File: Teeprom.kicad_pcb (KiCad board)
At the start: 2 copper layers, 16 x 38 mm, 4 parts, among them J1 Tandy_100_102_200_option_rom, U1 28C256

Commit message: improve pour
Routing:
- net /A10: track 22.2 -> 20.9 mm
- net /A6: track 6.71 -> 6.08 mm
- net /VSS: vias 6 -> 5
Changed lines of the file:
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@@
     (thickness 1.6)
     (drawings 11)
-    (tracks 140)
+    (tracks 137)
     (zones 0)
     (modules 4)
@@
   (via (at 151.9184 99.822) (size 0.508) (drill 0.254) (layers Top Bottom) (net 2))
   (segment (start 138.811 85.217) (end 138.7094 85.217) (width 0.2032) (layer Bottom) (net 2))
-  (segment (start 150.368 99.822) (end 144.0942 93.5482) (width 0.2032) (layer Bottom) (net 2))
-  (segment (start 144.0942 93.5482) (end 142.0876 93.5482) (width 0.2032) (layer Bottom) (net 2))
-  (segment (start 151.9184 99.822) (end 150.368 99.822) (width 0.2032) (layer Bottom) (net 2))
+  (segment (start 151.9184 99.822) (end 150.6474 99.822) (width 0.2032) (layer Bottom) (net 2))
   (segment (start 141.4526 87.8586) (end 138.811 85.217) (width 0.2032) (layer Bottom) (net 2))
-  (segment (start 142.0876 93.5482) (end 141.4526 92.9132) (width 0.2032) (layer Bottom) (net 2))
-  (segment (start 141.4526 92.9132) (end 141.4526 87.8586) (width 0.2032) (layer Bottom) (net 2))
+  (segment (start 141.4526 90.6272) (end 141.4526 87.8586) (width 0.2032) (layer Bottom) (net 2))
+  (segment (start 150.6474 99.822) (end 141.4526 90.6272) (width 0.2032) (layer Bottom) (net 2))
   (via (at 151.9174 106.172) (size 0.508) (drill 0.254) (layers Top Bottom) (net 3))
   (segment (start 151.9174 109.4613) (end 151.9174 106.172) (width 0.2032) (layer Bottom) (net 3))
@@
   (segment (start 155.575 110.617) (end 153.7462 108.7882) (width 0.2032) (layer Top) (net 5))
   (via (at 142.5194 94.742) (size 0.508) (drill 0.254) (layers Top Bottom) (net 6))
-  (segment (start 140.4747 93.7768) (end 141.4399 94.742) (width 0.2032) (layer Bottom) (net 6))
-  (segment (start 140.4747 91.96705) (end 140.4747 93.7768) (width 0.2032) (layer Bottom) (net 6))
+  (segment (start 140.716 92.9386) (end 142.5194 94.742) (width 0.2032) (layer Bottom) (net 6))
+  (segment (start 140.716 92.20835) (end 140.716 92.9386) (width 0.2032) (layer Bottom) (net 6))
   (segment (start 138.7094 90.297) (end 138.80465 90.297) (width 0.2032) (layer Bottom) (net 6))
-  (segment (start 141.4399 94.742) (end 142.5194 94.742) (width 0.2032) (layer Bottom) (net 6))
-  (segment (start 138.80465 90.297) (end 140.4747 91.96705) (width 0.2032) (layer Bottom) (net 6))
+  (segment (start 138.80465 90.297) (end 140.716 92.20835) (width 0.2032) (layer Bottom) (net 6))
   (via (at 151.9174 103.632) (size 0.508) (drill 0.254) (layers Top Bottom) (net 7))
   (segment (start 153.6065 105.3211) (end 151.9174 103.632) (width 0.2032) (layer Bottom) (net 7))
@@
   (segment (start 138.7094 105.537) (end 138.8745 105.537) (width 0.2032) (layer Top) (net 17))
   (segment (start 138.8745 105.537) (end 140.6906 103.7209) (width 0.2032) (layer Top) (net 17))
-  (via (at 142.5184 92.202) (size 0.508) (drill 0.254) (layers Top Bottom) (net 18))
   (segment (start 155.0924 92.202) (end 155.7274 92.837) (width 0.2032) (layer Bottom) (net 18))
-  (segment (start 142.5184 92.202) (end 155.0924 92.202) (width 0.2032) (layer Bottom) (net 18))
+  (via (at 145.9484 92.202) (size 0.508) (drill 0.254) (layers Top Bottom) (net 18))
+  (segment (start 145.9484 92.202) (end 155.0924 92.202) (width 0.2032) (layer Bottom) (net 18))
+  (segment (start 142.5184 92.202) (end 145.9484 92.202) (width 0.2032) (layer Top) (net 18))
   (via (at 142.5194 103.632) (size 0.508) (drill 0.254) (layers Top Bottom) (net 19))
   (segment (start 141.0208 105.1306) (end 142.5194 103.632) (width 0.2032) (layer Bottom) (net 19))
@@
   (segment (start 155.1199 85.9155) (end 149.1107 85.9155) (width 0.2032) (layer Top) (net 24))
   (segment (start 148.0058 87.0204) (end 148.0058 98.3742) (width 0.2032) (layer Top) (net 24))
-  (segment (start 155.0289 83.3755) (end 149.5679 83.3755) (width 0.2032) (layer Top) (net 25))
+  (segment (start 143.5481 90.932) (end 142.5184 90.932) (width 0.2032) (layer Top) (net 25))
+  (segment (start 149.8346 83.3755) (end 143.9164 89.2937) (width 0.2032) (layer Top) (net 25))
+  (segment (start 155.0289 83.3755) (end 149.8346 83.3755) (width 0.2032) (layer Top) (net 25))
+  (segment (start 143.9164 89.2937) (end 143.9164 90.5637) (width 0.2032) (layer Top) (net 25))
   (segment (start 155.7274 82.677) (end 155.0289 83.3755) (width 0.2032) (layer Top) (net 25))
-  (segment (start 149.5679 83.3755) (end 146.5072 86.4362) (width 0.2032) (layer Top) (net 25))
-  (segment (start 143.5481 90.932) (end 142.5184 90.932) (width 0.2032) (layer Top) (net 25))
-  (segment (start 146.5072 87.9729) (end 143.5481 90.932) (width 0.2032) (layer Top) (net 25))
-  (segment (start 146.5072 86.4362) (end 146.5072 87.9729) (width 0.2032) (layer Top) (net 25))
+  (segment (start 143.9164 90.5637) (end 143.5481 90.932) (width 0.2032) (layer Top) (net 25))
   (segment (start 150.5991 89.1007) (end 150.5991 88.7984) (width 0.2032) (layer Top) (net 26))
   (segment (start 150.3553 89.3445) (end 150.5991 89.1007) (width 0.2032) (layer Top) (net 26))
@@
   (segment (start 151.9184 92.202) (end 150.9268 92.202) (width 0.2032) (layer Top) (net 26))
   (segment (start 150.9268 92.202) (end 150.3553 91.6305) (width 0.2032) (layer Top) (net 26))
-  (via (at 151.5491 89.9795) (size 0.508) (drill 0.254) (layers Top Bottom) (net 27))
   (via (at 149.7584 96.647) (size 0.508) (drill 0.254) (layers Top Bottom) (net 27))
-  (via (at 147.2184 106.807) (size 0.508) (drill 0.254) (layers Top Bottom) (net 27))
   (via (at 147.2184 82.677) (size 0.508) (drill 0.254) (layers Top Bottom) (net 27))
   (segment (start 142.5184 112.1547) (end 142.5184 107.442) (width 0.4064) (layer Top) (net 27))
   (segment (start 138.7094 115.697) (end 138.9761 115.697) (width 0.4064) (layer Top) (net 27))
   (segment (start 138.9761 115.697) (end 142.5184 112.1547) (width 0.4064) (layer Top) (net 27))
-  (via (at 147.2184 93.472) (size 0.508) (drill 0.254) (layers Top Bottom) (net 27))
-  (via (at 147.2184 89.027) (size 0.508) (drill 0.254) (layers Top Bottom) (net 27))
+  (via (at 147.2184 94.107) (size 0.508) (drill 0.254) (layers Top Bottom) (net 27))
+  (via (at 147.2184 87.757) (size 0.508) (drill 0.254) (layers Top Bottom) (net 27))
+  (via (at 151.5491 89.9414) (size 0.508) (drill 0.254) (layers Top Bottom) (net 27))
   (via (at 151.9184 90.932) (size 0.508) (drill 0.254) (layers Top Bottom) (net 28))
   (segment (start 138.9761 82.677) (end 138.6184 82.677) (width 0.4064) (layer Bottom) (net 28))

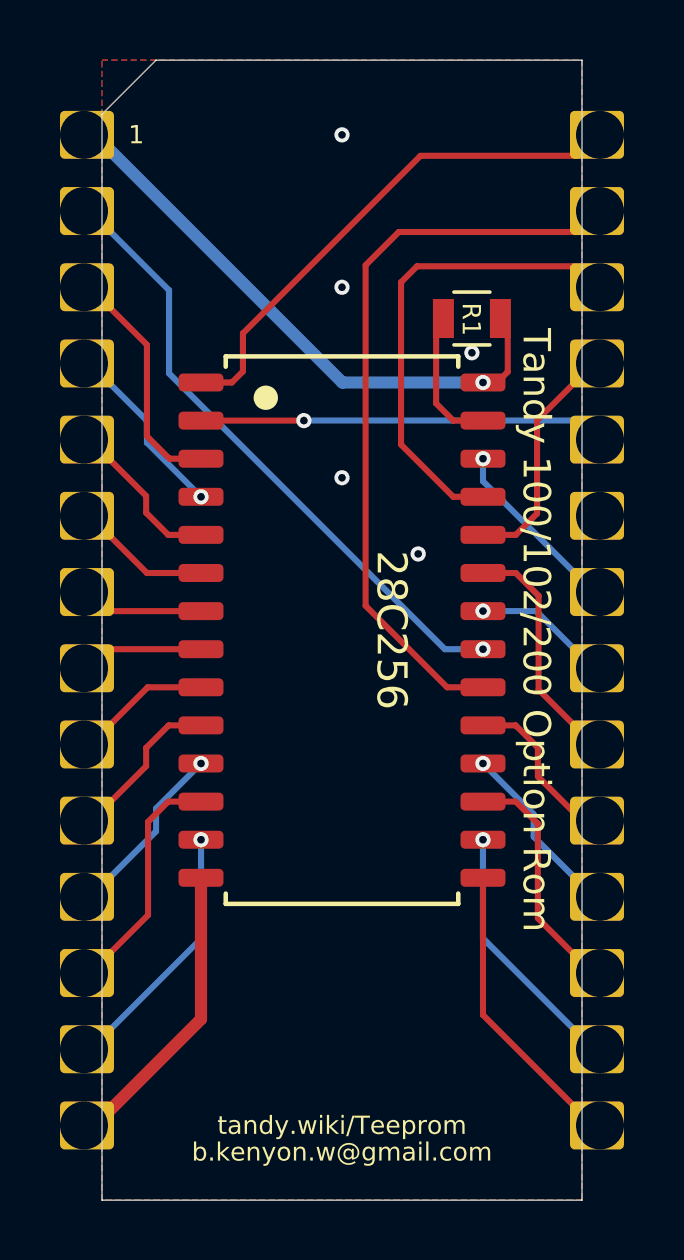
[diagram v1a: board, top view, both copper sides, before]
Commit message: improve ground paths in pours
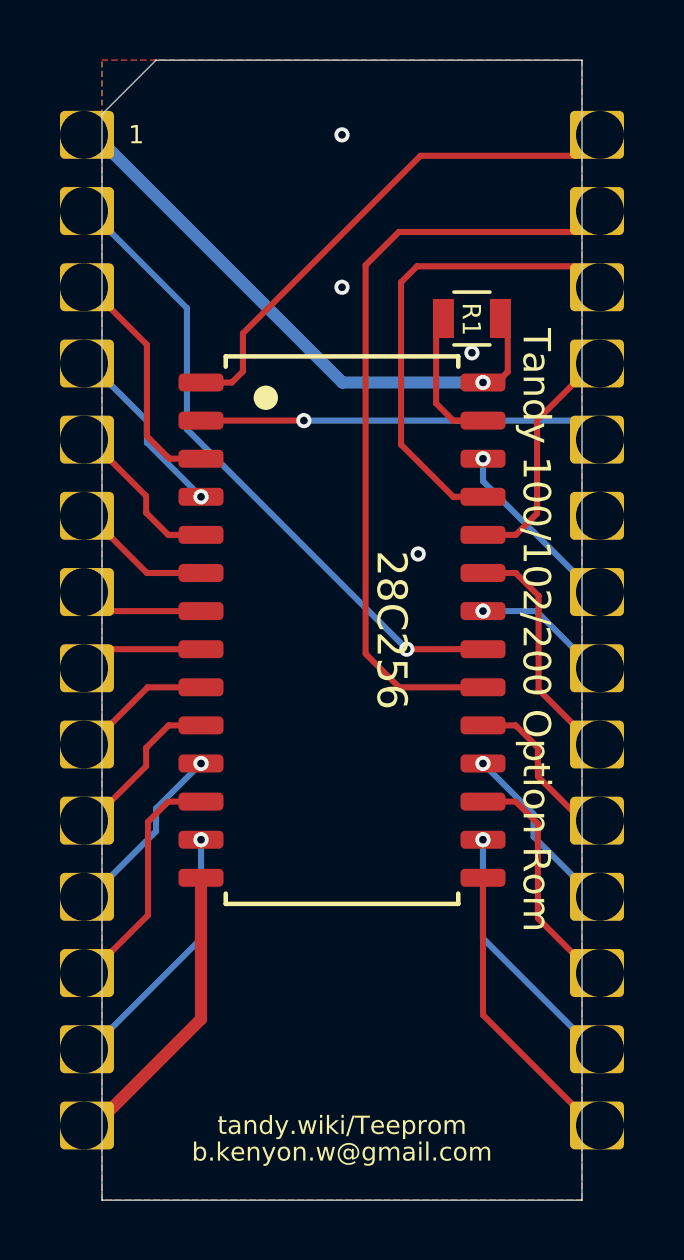
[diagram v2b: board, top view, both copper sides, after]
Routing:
- net /~CE: track 24.9 -> 25.9 mm
- net /A10: track 20.9 -> 21.6 mm
- net /VSS: vias 5 -> 4
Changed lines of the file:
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@@
     (thickness 1.6)
     (drawings 11)
-    (tracks 137)
+    (tracks 136)
     (zones 0)
     (modules 4)
@@
   (segment (start 155.7274 115.697) (end 155.6004 115.697) (width 0.2032) (layer Top) (net 1))
   (segment (start 155.6004 115.697) (end 151.9184 112.015) (width 0.2032) (layer Top) (net 1))
-  (via (at 151.9184 99.822) (size 0.508) (drill 0.254) (layers Top Bottom) (net 2))
+  (via (at 149.3774 99.822) (size 0.508) (drill 0.254) (layers Top Bottom) (net 2))
+  (segment (start 151.9184 99.822) (end 149.3774 99.822) (width 0.2032) (layer Top) (net 2))
   (segment (start 138.811 85.217) (end 138.7094 85.217) (width 0.2032) (layer Bottom) (net 2))
-  (segment (start 151.9184 99.822) (end 150.6474 99.822) (width 0.2032) (layer Bottom) (net 2))
-  (segment (start 141.4526 87.8586) (end 138.811 85.217) (width 0.2032) (layer Bottom) (net 2))
-  (segment (start 141.4526 90.6272) (end 141.4526 87.8586) (width 0.2032) (layer Bottom) (net 2))
-  (segment (start 150.6474 99.822) (end 141.4526 90.6272) (width 0.2032) (layer Bottom) (net 2))
+  (segment (start 149.3774 99.822) (end 142.0495 92.4941) (width 0.2032) (layer Bottom) (net 2))
+  (segment (start 142.0495 88.4555) (end 138.811 85.217) (width 0.2032) (layer Bottom) (net 2))
+  (segment (start 142.0495 92.4941) (end 142.0495 88.4555) (width 0.2032) (layer Bottom) (net 2))
   (via (at 151.9174 106.172) (size 0.508) (drill 0.254) (layers Top Bottom) (net 3))
   (segment (start 151.9174 109.4613) (end 151.9174 106.172) (width 0.2032) (layer Bottom) (net 3))
@@
   (segment (start 138.7094 113.157) (end 138.8364 113.157) (width 0.2032) (layer Bottom) (net 23))
   (segment (start 138.8364 113.157) (end 142.5194 109.474) (width 0.2032) (layer Bottom) (net 23))
-  (segment (start 150.7236 101.092) (end 151.9184 101.092) (width 0.2032) (layer Top) (net 24))
-  (segment (start 148.0058 98.3742) (end 150.7236 101.092) (width 0.2032) (layer Top) (net 24))
+  (segment (start 149.1234 101.092) (end 151.9184 101.092) (width 0.2032) (layer Top) (net 24))
   (segment (start 155.7274 85.308) (end 155.1199 85.9155) (width 0.2032) (layer Top) (net 24))
+  (segment (start 148.0058 99.9744) (end 149.1234 101.092) (width 0.2032) (layer Top) (net 24))
+  (segment (start 148.0058 87.0204) (end 148.0058 99.9744) (width 0.2032) (layer Top) (net 24))
   (segment (start 155.7274 85.217) (end 155.7274 85.308) (width 0.2032) (layer Top) (net 24))
   (segment (start 149.1107 85.9155) (end 148.0058 87.0204) (width 0.2032) (layer Top) (net 24))
   (segment (start 155.1199 85.9155) (end 149.1107 85.9155) (width 0.2032) (layer Top) (net 24))
-  (segment (start 148.0058 87.0204) (end 148.0058 98.3742) (width 0.2032) (layer Top) (net 24))
   (segment (start 143.5481 90.932) (end 142.5184 90.932) (width 0.2032) (layer Top) (net 25))
   (segment (start 149.8346 83.3755) (end 143.9164 89.2937) (width 0.2032) (layer Top) (net 25))
@@
   (segment (start 138.7094 115.697) (end 138.9761 115.697) (width 0.4064) (layer Top) (net 27))
   (segment (start 138.9761 115.697) (end 142.5184 112.1547) (width 0.4064) (layer Top) (net 27))
-  (via (at 147.2184 94.107) (size 0.508) (drill 0.254) (layers Top Bottom) (net 27))
   (via (at 147.2184 87.757) (size 0.508) (drill 0.254) (layers Top Bottom) (net 27))
   (via (at 151.5491 89.9414) (size 0.508) (drill 0.254) (layers Top Bottom) (net 27))
